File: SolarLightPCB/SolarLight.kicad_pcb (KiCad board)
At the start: 2 copper layers, 100 x 45 mm, 17 parts, among them J1 I2C, J2 SPI, U1 TP4056, U2 WeMos_D1_mini, U3 MCP1700-3302E

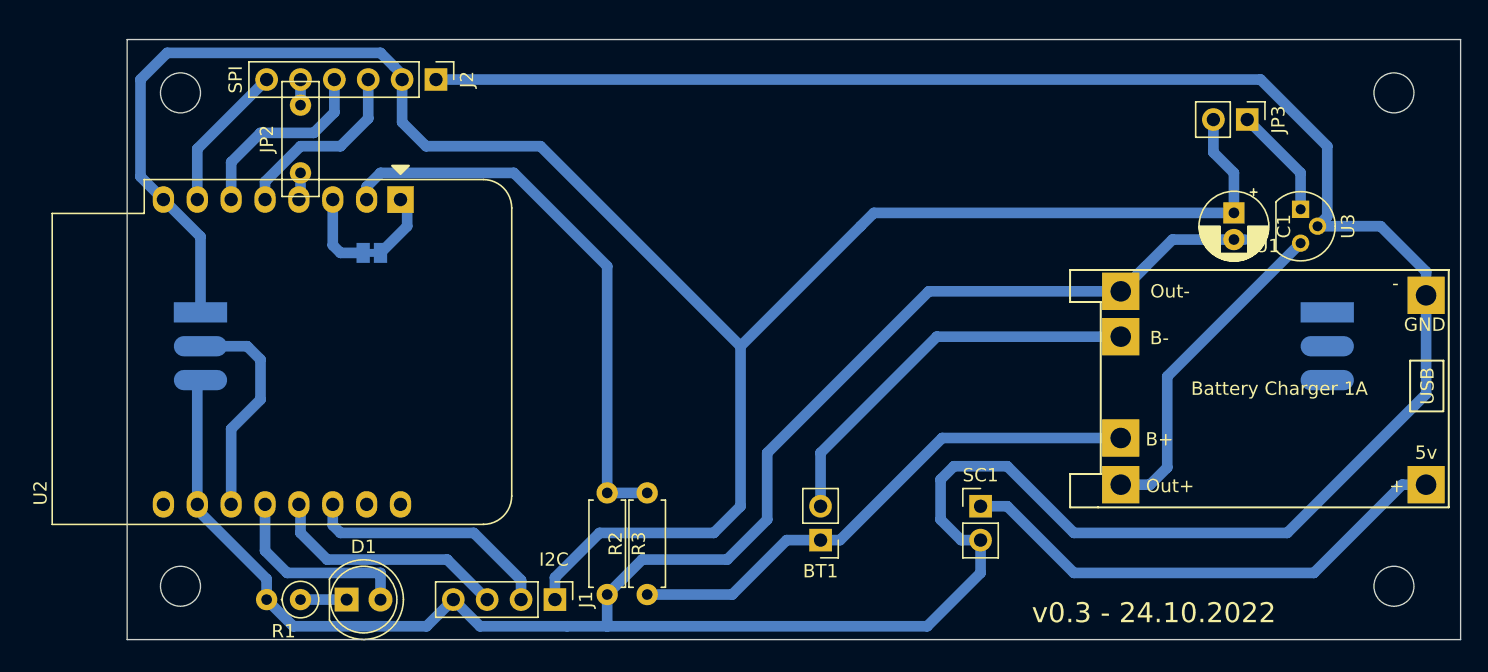
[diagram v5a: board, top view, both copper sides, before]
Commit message: PCB Improvements
- Bigger Package for the voltage regulator
- Only one trace per pad (prefer to merge in the track instead)
- Specify some minimal trace distance
- Finer grid for the PCB to allow for better routing (5mils)
- Cleanup unconnected traces
- Ignore non-relevant DRC warnings
- Run DRC
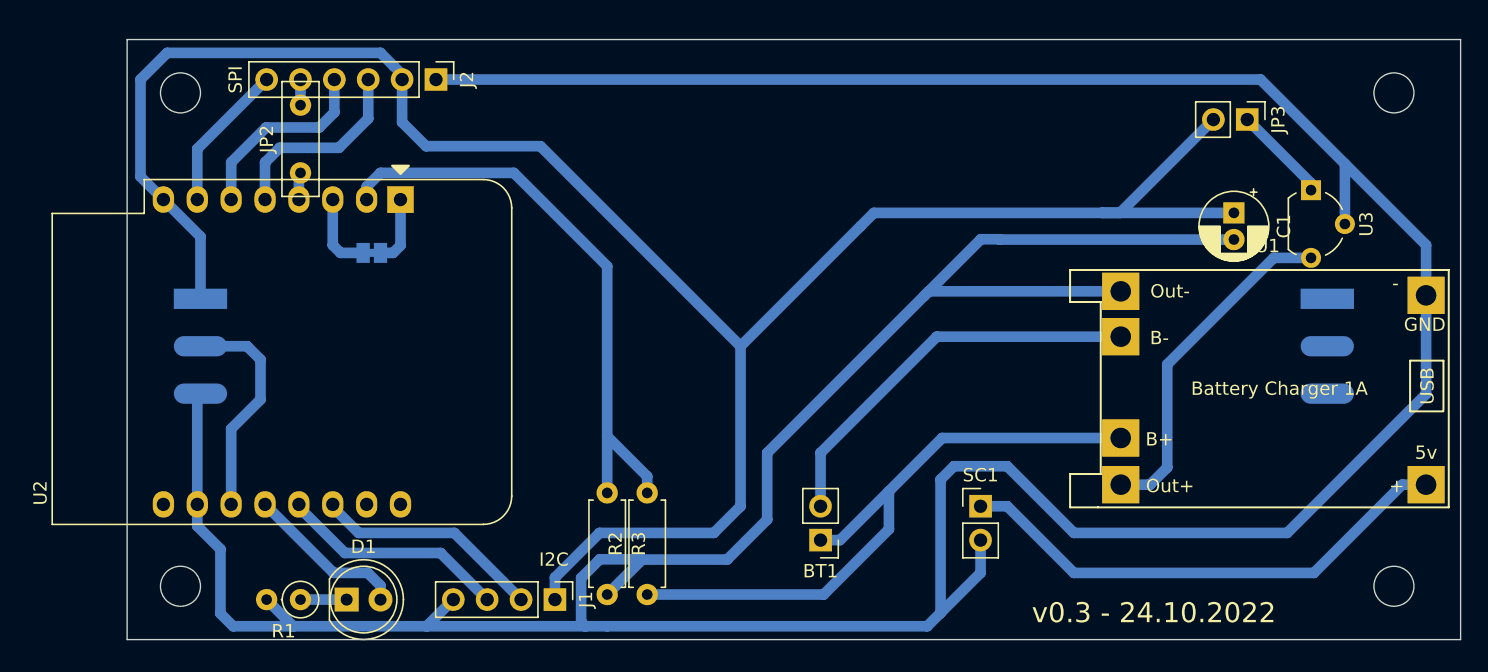
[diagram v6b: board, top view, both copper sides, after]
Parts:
- U3: footprint Package_TO_SOT_THT:TO-92 -> Package_TO_SOT_THT:TO-92L_Wide
- moved U3 1.64 mm to (168.8, 66.3)
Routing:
- net GND: track 290.5 -> 317.6 mm
- net BATTERY: track 40.4 -> 48.7 mm
- net +3V3: track 155.3 -> 157.9 mm
- net LED: track 14.8 -> 12.2 mm
- net A0: track 42.3 -> 44.8 mm
- net SCL: track 18.8 -> 17.2 mm
- net Net-(U3-Pad1): track 8.39 -> 7.28 mm
- net SDA: track 18.3 -> 17.2 mm
- net Net-(U1-Pad3): track 25.0 -> 25.8 mm
- net MISO: track 14.0 -> 14.8 mm
- net RST: track 5.74 -> 5.17 mm

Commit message: Add the output of the neopixel pin to GND
For now not the 3.3V since it’s hard to route that one over there
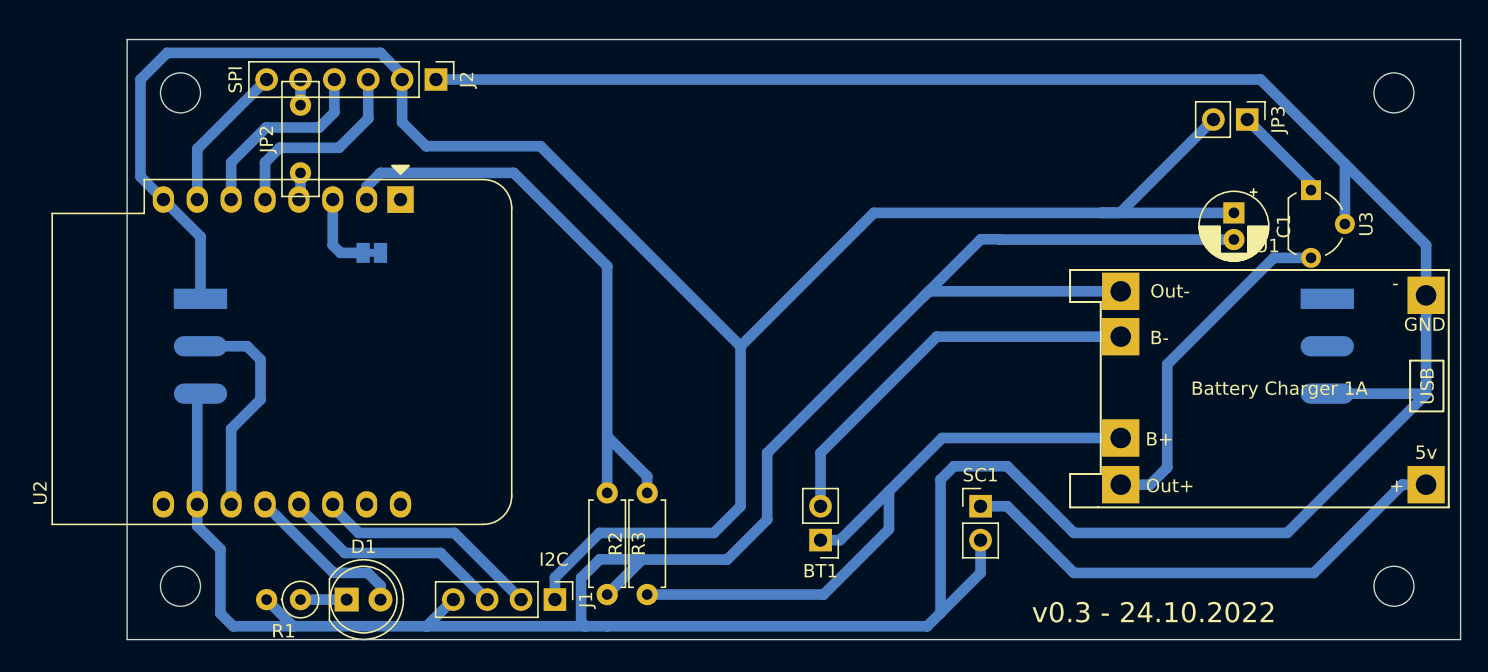
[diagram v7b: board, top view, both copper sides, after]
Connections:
- LIN1 pad 3: unconnected-(LIN1-Pad3) -> GND
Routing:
- net GND: track 317.6 -> 326.2 mm
- net RST: track 5.17 -> 0.71 mm

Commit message: Fix wrong pin numbering on the 3.3 voltage regulator
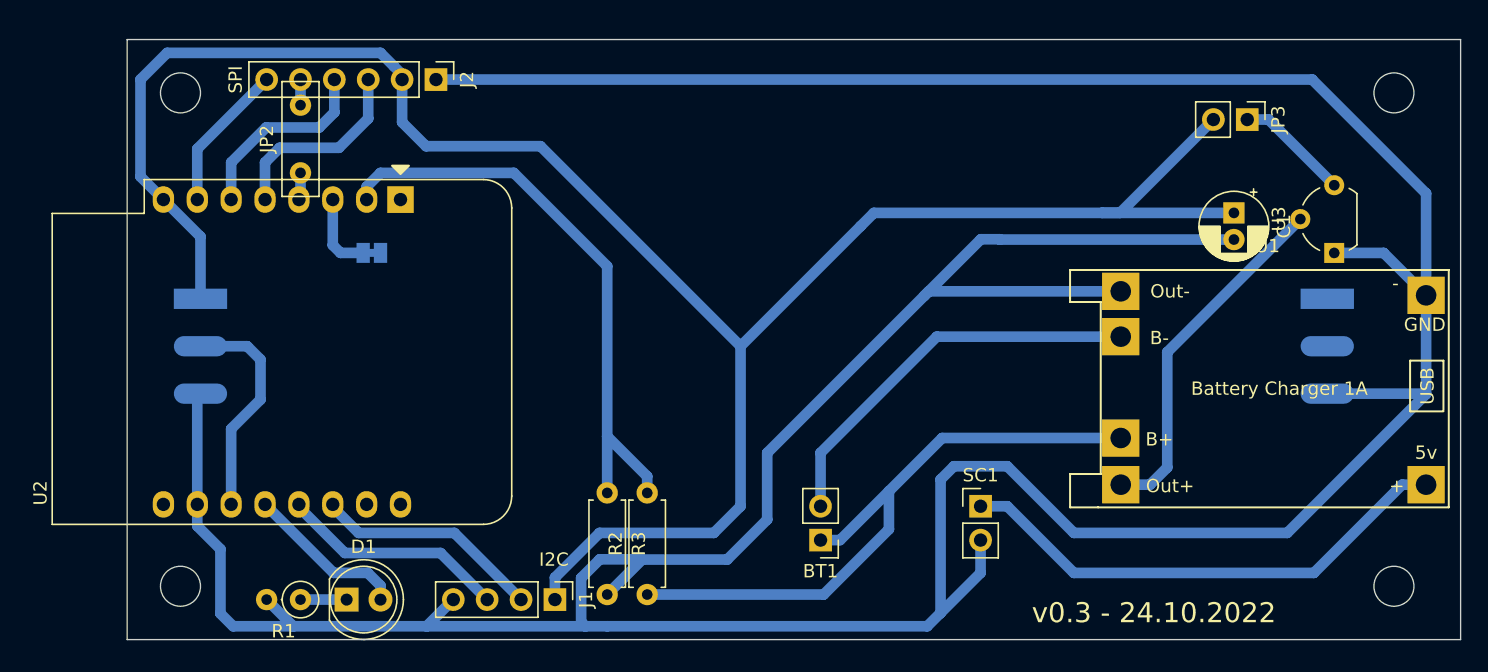
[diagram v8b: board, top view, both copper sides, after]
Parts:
- moved U3 5.02 mm to (170.5, 71.0), turned to 90 degrees
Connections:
- JP3 pad 1: Net-(U3-Pad1) -> Net-(JP3-Pad1)
- U3 pad 1: Net-(U3-Pad1) -> GND
- U3 pad 2: GND -> Net-(U1-Pad3)
- U3 pad 3: Net-(U1-Pad3) -> Net-(JP3-Pad1)
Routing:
- net Net-(JP3-Pad1): track 0.00 -> 8.56 mm
- net Net-(U3-Pad1): track 7.28 -> 0.00 mm
- net GND: track 326.2 -> 332.2 mm
- net Net-(U1-Pad3): track 25.8 -> 26.8 mm
